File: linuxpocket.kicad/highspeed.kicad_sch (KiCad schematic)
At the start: 5 parts, among them J2 Bus_PCI_Express_Mini

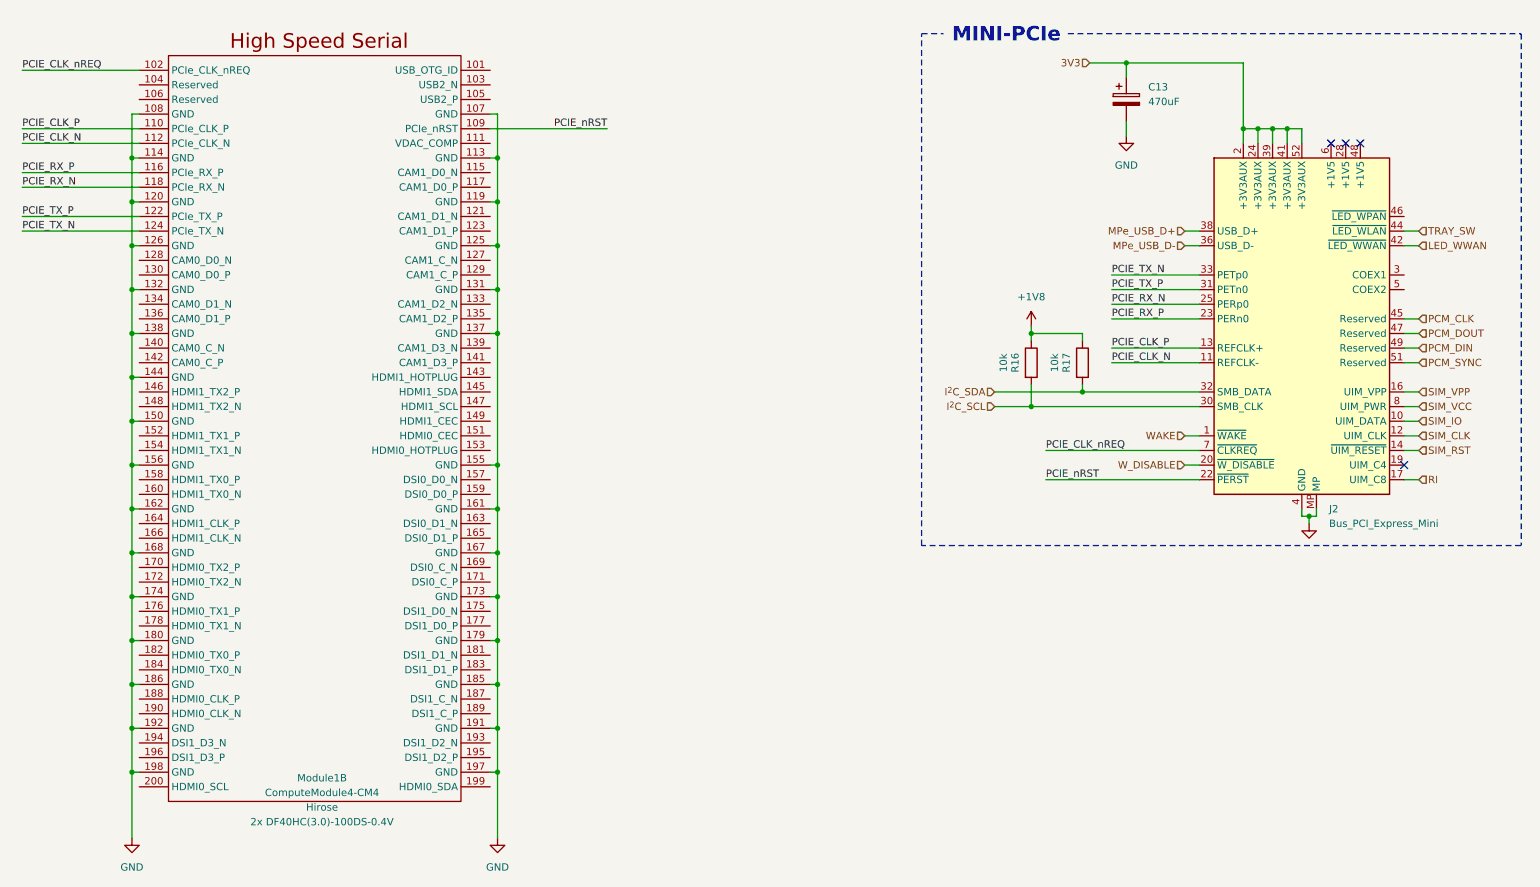
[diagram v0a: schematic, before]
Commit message: Add keyboard, improve many things etc.
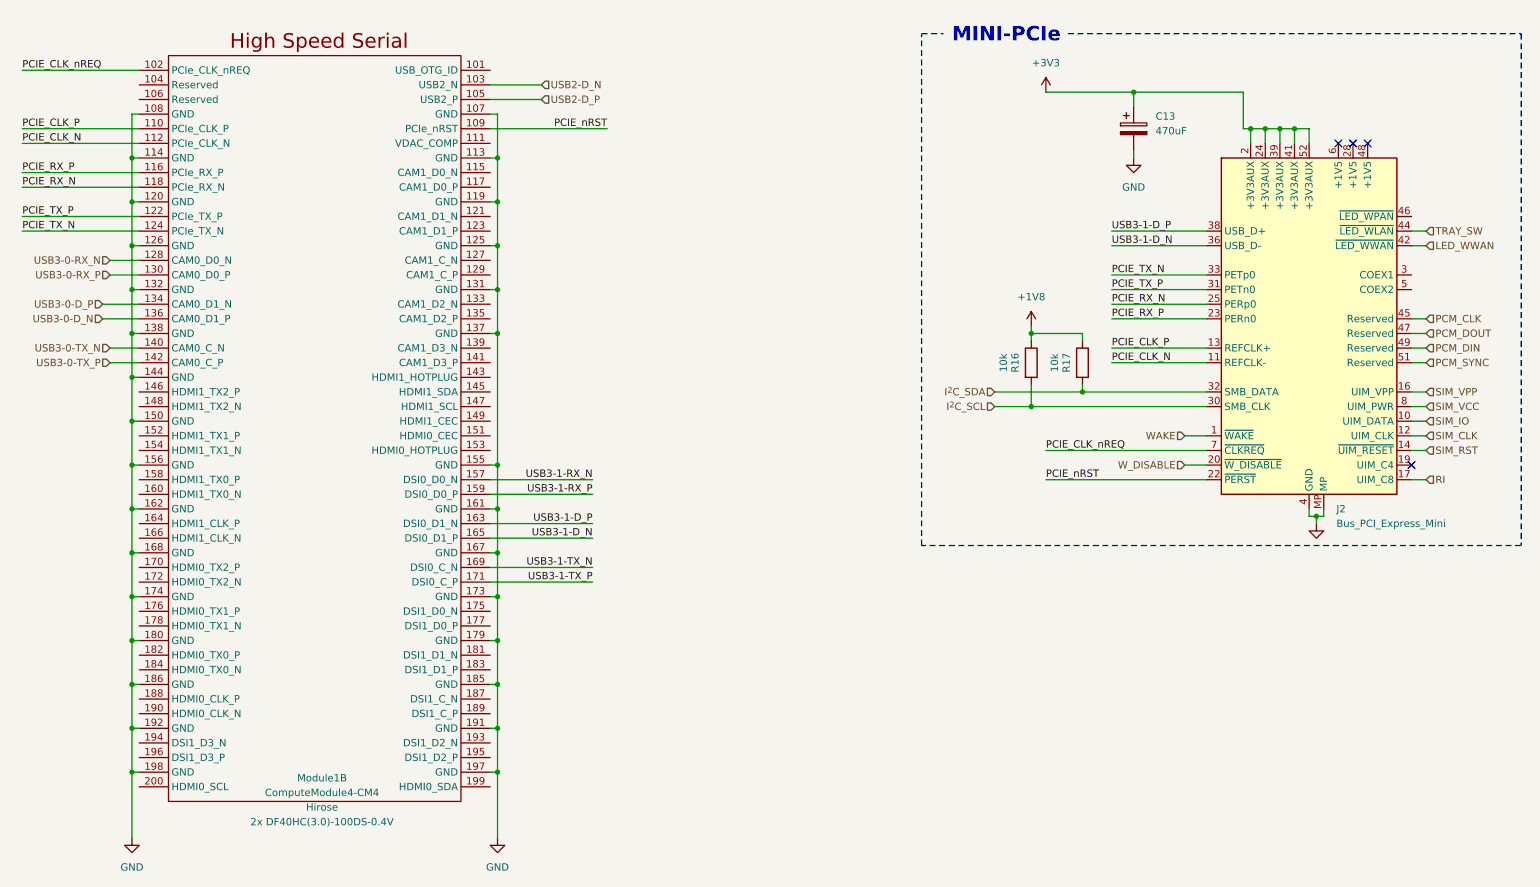
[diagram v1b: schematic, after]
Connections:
- net MPe_USB_D+ is gone; now on net USB3-1-D_P: J2.38 (USB_D+)
- net MPe_USB_D- is gone; now on net USB3-1-D_N: J2.36 (USB_D-)
- net USB2-D_N: now reaches Module1.103 (USB2_N)
- net USB2-D_P: now reaches Module1.105 (USB2_P)
- net USB3-0-RX_N: now reaches Module1.128 (CAM0_D0_N)
- net USB3-0-RX_P: now reaches Module1.130 (CAM0_D0_P)
- net USB3-0-D_P: now reaches Module1.134 (CAM0_D1_N)
- net USB3-0-D_N: now reaches Module1.136 (CAM0_D1_P)
- net USB3-0-TX_N: now reaches Module1.140 (CAM0_C_N)
- net USB3-0-TX_P: now reaches Module1.142 (CAM0_C_P)
- net USB3-1-RX_N: now reaches Module1.157 (DSI0_D0_N)
- net USB3-1-RX_P: now reaches Module1.159 (DSI0_D0_P)
- net USB3-1-D_P: now reaches Module1.163 (DSI0_D1_N)
- net USB3-1-D_N: now reaches Module1.165 (DSI0_D1_P)
- net USB3-1-TX_N: now reaches Module1.169 (DSI0_C_N)
- net USB3-1-TX_P: now reaches Module1.171 (DSI0_C_P)
- net 3V3 renamed +3V3
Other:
- moved on the sheet: C13, J2

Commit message: Start with HDMI connector.
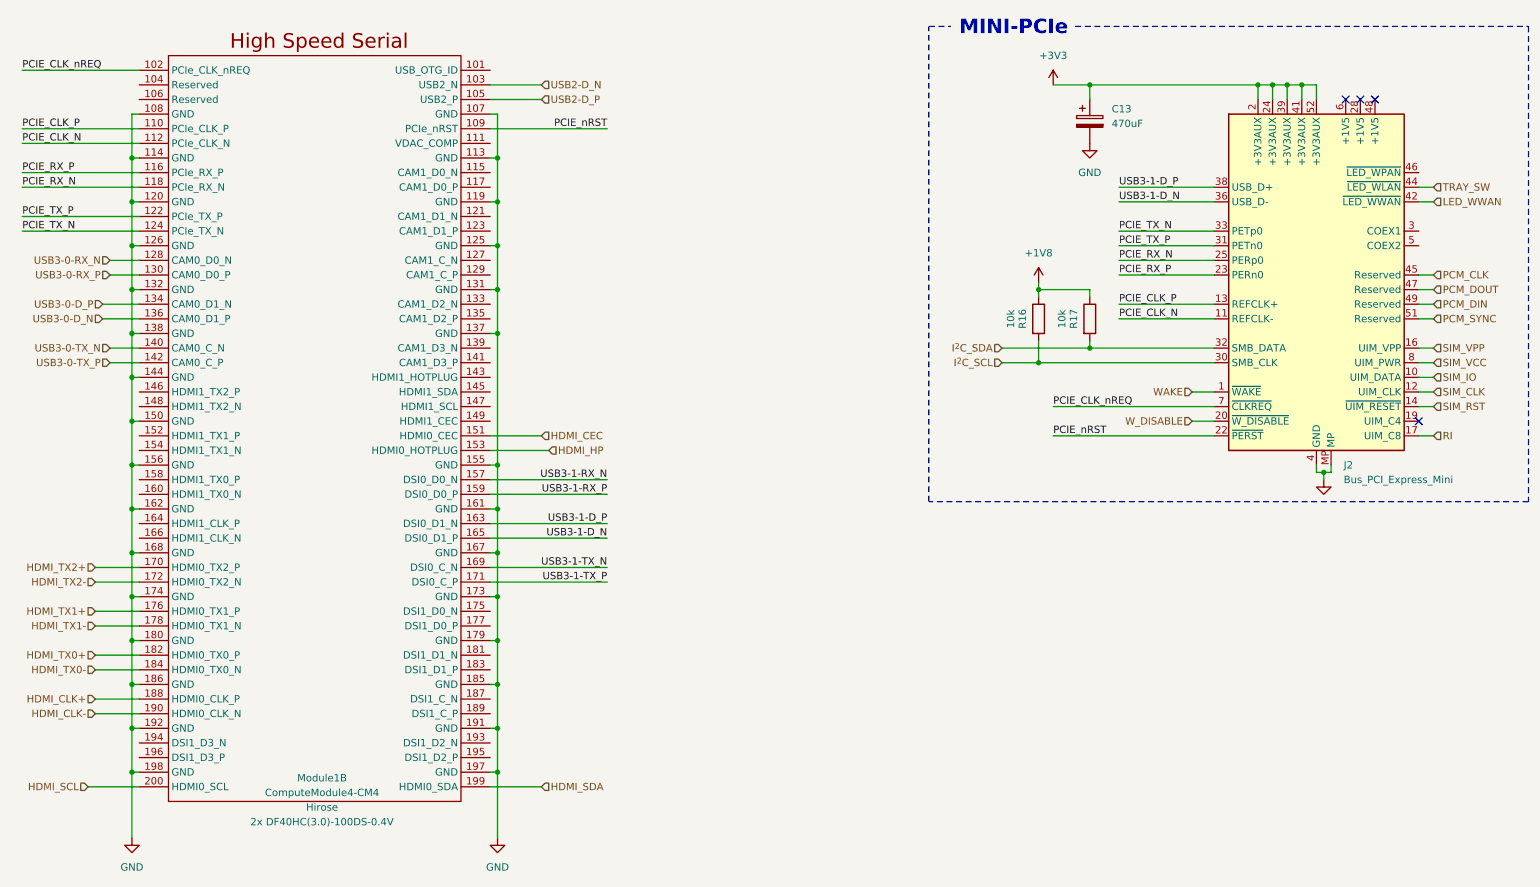
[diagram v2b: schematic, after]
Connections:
- net HDMI_CEC: now reaches Module1.151 (HDMI0_CEC)
- net HDMI_HP: now reaches Module1.153 (HDMI0_HOTPLUG)
- net HDMI_TX2+: now reaches Module1.170 (HDMI0_TX2_P)
- net HDMI_TX2-: now reaches Module1.172 (HDMI0_TX2_N)
- net HDMI_TX1+: now reaches Module1.176 (HDMI0_TX1_P)
- net HDMI_TX1-: now reaches Module1.178 (HDMI0_TX1_N)
- net HDMI_TX0+: now reaches Module1.182 (HDMI0_TX0_P)
- net HDMI_TX0-: now reaches Module1.184 (HDMI0_TX0_N)
- net HDMI_CLK+: now reaches Module1.188 (HDMI0_CLK_P)
- net HDMI_CLK-: now reaches Module1.190 (HDMI0_CLK_N)
- net HDMI_SDA: now reaches Module1.199 (HDMI0_SDA)
- net HDMI_SCL: now reaches Module1.200 (HDMI0_SCL)
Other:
- moved on the sheet: C13, J2, R16, R17

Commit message: Add magnetometer #5. Add footprints to some symbols.
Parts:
- C13: footprint (none) -> Capacitor_Tantalum_SMD:CP_EIA-7343-31_Kemet-D; LCSC (none) -> C123270
- J2: footprint (none) -> Connector_PCBEdge:BUS_PCI_Express_Mini
- R16, R17: footprint (none) -> Resistor_SMD:R_0402_1005Metric; LCSC (none) -> C25744
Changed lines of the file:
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@@
+	)
+	(symbol
+		(lib_id "Device:C_Polarized")
+		(at 204.47 33.02 0)
+		(unit 1)
+		(exclude_from_sim no)
+		(in_bom yes)
+		(on_board yes)
+		(dnp no)
+		(fields_autoplaced yes)
+		(property "Reference" "C13"
+			(at 208.28 30.8609 0)
+			(effects
+				(font
+					(size 1.27 1.27)
+				)
+				(justify left)
+			)
+		)
+		(property "Value" "470uF"
+			(at 208.28 33.4009 0)
+			(effects
+				(font
+					(size 1.27 1.27)
+				)
+				(justify left)
+			)
+		)
+		(property "Footprint" "Capacitor_Tantalum_SMD:CP_EIA-7343-31_Kemet-D"
+			(at 205.4352 36.83 0)
+			(effects
+				(font
+					(size 1.27 1.27)
+				)
+				(hide yes)
+			)
+		)
+		(property "Datasheet" "~"
+			(at 204.47 33.02 0)
+			(effects
+				(font
+					(size 1.27 1.27)
+				)
+				(hide yes)
+			)
+		)
+		(property "Description" "Polarized capacitor"
+			(at 204.47 33.02 0)
+			(effects
+				(font
+					(size 1.27 1.27)
+				)
+				(hide yes)
+			)
+		)
+		(property "LCSC" "C123270"
+			(at 204.47 33.02 0)
+			(effects
+				(font
+					(size 1.27 1.27)
+				)
+				(hide yes)
+			)
+		)
+		(pin "1"
+		)
+		(pin "2"
+		)
+		(instances
+			(project "linuxpocket"
+				(path "/de3771bf-b13a-459d-a957-6ff90f7da387/7405f2ae-4443-4e6f-9c19-b00d1eeb9817"
+					(reference "C13")
+					(unit 1)
+				)
+			)
+		)
 	)
 	(symbol
@@
 			)
 		)
-		(property "Footprint" ""
+		(property "Footprint" "Connector_PCBEdge:BUS_PCI_Express_Mini"
 			(at 243.84 62.23 0)
 			(effects
@@
 			)
 		)
-		(property "Footprint" ""
+		(property "Footprint" "Resistor_SMD:R_0402_1005Metric"
 			(at 193.802 67.31 90)
 			(effects
@@
 		(property "Description" "Resistor"
 			(at 195.58 67.31 0)
+			(effects
+				(font
+					(size 1.27 1.27)
+				)
+				(hide yes)
+			)
+		)
+		(property "LCSC" "C25744"
+			(at 195.58 67.31 90)
 			(effects
 				(font
@@
 				(path "/de3771bf-b13a-459d-a957-6ff90f7da387/7405f2ae-4443-4e6f-9c19-b00d1eeb9817"
 					(reference "R16")
-					(unit 1)
-				)
-			)
-		)
-	)
-	(symbol
-		(lib_id "Device:C_Polarized")
-		(at 204.47 33.02 0)
-		(unit 1)
-		(exclude_from_sim no)
-		(in_bom yes)
-		(on_board yes)
-		(dnp no)
-		(fields_autoplaced yes)
-		(property "Reference" "C13"
-			(at 208.28 30.8609 0)
-			(effects
-				(font
-					(size 1.27 1.27)
-				)
-				(justify left)
-			)
-		)
-		(property "Value" "470uF"
-			(at 208.28 33.4009 0)
-			(effects
-				(font
-					(size 1.27 1.27)
-				)
-				(justify left)
-			)
-		)
-		(property "Footprint" ""
-			(at 205.4352 36.83 0)
-			(effects
-				(font
-					(size 1.27 1.27)
-				)
-				(hide yes)
-			)
-		)
-		(property "Datasheet" "~"
-			(at 204.47 33.02 0)
-			(effects
-				(font
-					(size 1.27 1.27)
-				)
-				(hide yes)
-			)
-		)
-		(property "Description" "Polarized capacitor"
-			(at 204.47 33.02 0)
-			(effects
-				(font
-					(size 1.27 1.27)
-				)
-				(hide yes)
-			)
-		)
-		(pin "1"
-		)
-		(pin "2"
-		)
-		(instances
-			(project "linuxpocket"
-				(path "/de3771bf-b13a-459d-a957-6ff90f7da387/7405f2ae-4443-4e6f-9c19-b00d1eeb9817"
-					(reference "C13")
 					(unit 1)
 				)
@@
 			)
 		)
-		(property "Footprint" ""
+		(property "Footprint" "Resistor_SMD:R_0402_1005Metric"
 			(at 202.692 67.31 90)
 			(effects
@@
 			(effects
 				(font
+					(size 1.27 1.27)
+				)
+				(hide yes)
+			)
+		)
+		(property "LCSC" "C25744"
+			(at 204.47 67.31 90)
+			(effects
+				(font

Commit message: Start placing components in PCB.
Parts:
- J2: footprint Connector_PCBEdge:BUS_PCI_Express_Mini -> Connector_PCBEdge:BUS_PCI_Express_Mini_Full
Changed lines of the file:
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@@
 	(title_block
 		(title "High Speed Signals")
-		(date "2024-10-31")
+		(date "2024-10-31 - 2025-02-02")
 		(rev "Prototype v0")
 		(company "xamuel.xyz")
@@
 			)
 		)
-		(property "Footprint" "Connector_PCBEdge:BUS_PCI_Express_Mini"
+		(property "Footprint" "Connector_PCBEdge:BUS_PCI_Express_Mini_Full"
 			(at 243.84 62.23 0)
 			(effects

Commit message: PCB almost done and schematic finished.
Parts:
- removed R16, R17: 10k, Resistor_SMD:R_0402_1005Metric, symbol Device:R
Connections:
- net I^{2}C_SCL: no longer names the net of J2.30 (SMB_CLK)
- net I^{2}C_SDA: no longer names the net of J2.32 (SMB_DATA)
- no-connect marks 4 -> 42

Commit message: PCB basically finished.
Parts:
- Module1: LCSC C424649 -> C19089325
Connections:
- net PCIE_CLK_N: no longer J2.11 (REFCLK-)
- net PCIE_CLK_P: no longer J2.13 (REFCLK+)
- net PCIE_CLK_nREQ: no longer J2.7 (~{CLKREQ})
- net PCIE_RX_N: no longer J2.25 (PERp0)
- net PCIE_RX_P: no longer J2.23 (PERn0)
- net PCIE_TX_N: no longer J2.33 (PETp0)
- net PCIE_TX_P: no longer J2.31 (PETn0)
- net PCIE_nRST: no longer J2.22 (~{PERST})
- no-connect marks 42 -> 52
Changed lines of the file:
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@@
+	)
+	(no_connect
+		(at 226.06 52.07)
+	)
+	(no_connect
+		(at 226.06 64.77)
 	)
 	(no_connect
@@
 	)
 	(no_connect
+		(at 226.06 82.55)
+	)
+	(no_connect
 		(at 100.33 72.39)
 	)
@@
 	)
 	(no_connect
+		(at 261.62 52.07)
+	)
+	(no_connect
 		(at 39.37 105.41)
 	)
@@
 	)
 	(no_connect
+		(at 226.06 67.31)
+	)
+	(no_connect
 		(at 39.37 143.51)
 	)
@@
 	)
 	(no_connect
+		(at 226.06 87.63)
+	)
+	(no_connect
 		(at 100.33 125.73)
 	)
@@
 	)
 	(no_connect
+		(at 226.06 57.15)
+	)
+	(no_connect
 		(at 39.37 95.25)
 	)
@@
 	)
 	(no_connect
+		(at 261.62 54.61)
+	)
+	(no_connect
 		(at 100.33 67.31)
 	)
@@
 	)
 	(no_connect
+		(at 226.06 54.61)
+	)
+	(no_connect
 		(at 39.37 80.01)
 	)
 	(no_connect
+		(at 226.06 59.69)
+	)
+	(no_connect
 		(at 226.06 74.93)
 	)
@@
 	(wire
 		(pts
-			(xy 209.55 64.77) (xy 226.06 64.77)
-		)
-		(stroke
-			(width 0)
-			(type default)
-		)
-	)
-	(wire
-		(pts
 			(xy 38.1 39.37) (xy 39.37 39.37)
 		)
@@
 	(wire
 		(pts
-			(xy 209.55 52.07) (xy 226.06 52.07)
-		)
-		(stroke
-			(width 0)
-			(type default)
-		)
-	)
-	(wire
-		(pts
 			(xy 264.16 67.31) (xy 261.62 67.31)
 		)
@@
 	(wire
 		(pts
-			(xy 209.55 59.69) (xy 226.06 59.69)
-		)
-		(stroke
-			(width 0)
-			(type default)
-		)
-	)
-	(wire
-		(pts
 			(xy 100.33 97.79) (xy 120.65 97.79)
 		)
@@
 	(wire
 		(pts
-			(xy 198.12 82.55) (xy 226.06 82.55)
-		)
-		(stroke
-			(width 0)
-			(type default)
-		)
-	)
-	(wire
-		(pts
 			(xy 101.6 39.37) (xy 100.33 39.37)
 		)
@@
 	(wire
 		(pts
-			(xy 209.55 54.61) (xy 226.06 54.61)
-		)
-		(stroke
-			(width 0)
-			(type default)
-		)
-	)
-	(wire
-		(pts
 			(xy 19.05 41.91) (xy 39.37 41.91)
 		)
@@
 	(wire
 		(pts
-			(xy 198.12 87.63) (xy 226.06 87.63)
-		)
-		(stroke
-			(width 0)
-			(type default)
-		)
-	)
-	(wire
-		(pts
 			(xy 226.06 44.45) (xy 209.55 44.45)
 		)
@@
 	(wire
 		(pts
-			(xy 209.55 67.31) (xy 226.06 67.31)
-		)
-		(stroke
-			(width 0)
-			(type default)
-		)
-	)
-	(wire
-		(pts
 			(xy 38.1 138.43) (xy 38.1 130.81)
 		)
@@
 			(type default)
 			(color 0 0 0 1)
-		)
-	)
-	(wire
-		(pts
-			(xy 209.55 57.15) (xy 226.06 57.15)
-		)
-		(stroke
-			(width 0)
-			(type default)
 		)
 	)
@@
 			)
 		)
-		(property "LCSC" "C424649"
+		(property "LCSC" "C19089325"
 			(at -69.85 85.09 0)
 			(effects
